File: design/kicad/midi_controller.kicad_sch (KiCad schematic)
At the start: 1 part, among them U1 Teensy4.1

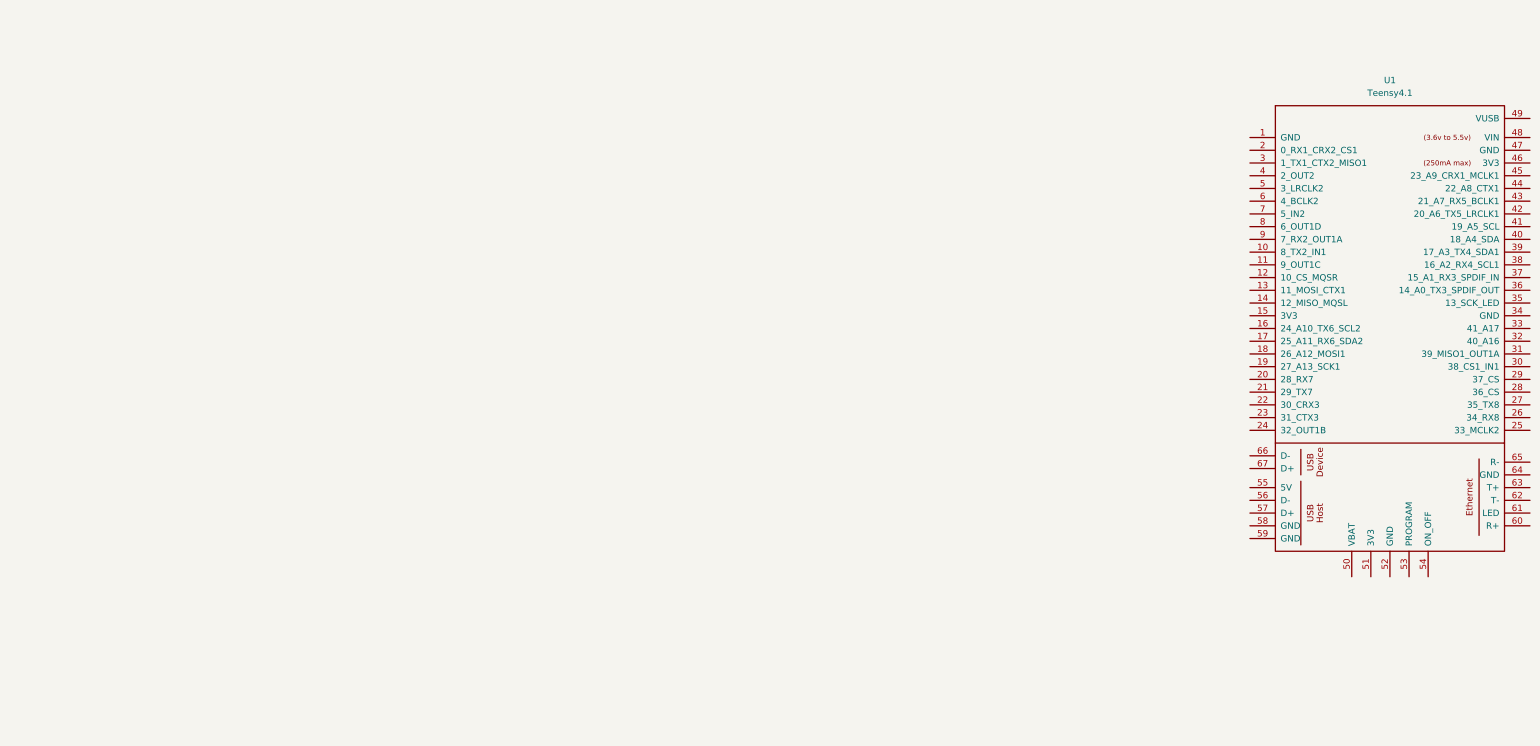
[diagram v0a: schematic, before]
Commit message: Add MIDI Controller component library to KiCad symbol library table
- Introduced a new symbol library for MIDI controllers located at
  "${KIPRJMOD}/component_library/midi_controller/midi_controller.kicad_sym".
- Updated the sym-lib-table to include the new library with a description
  for better organization and accessibility.
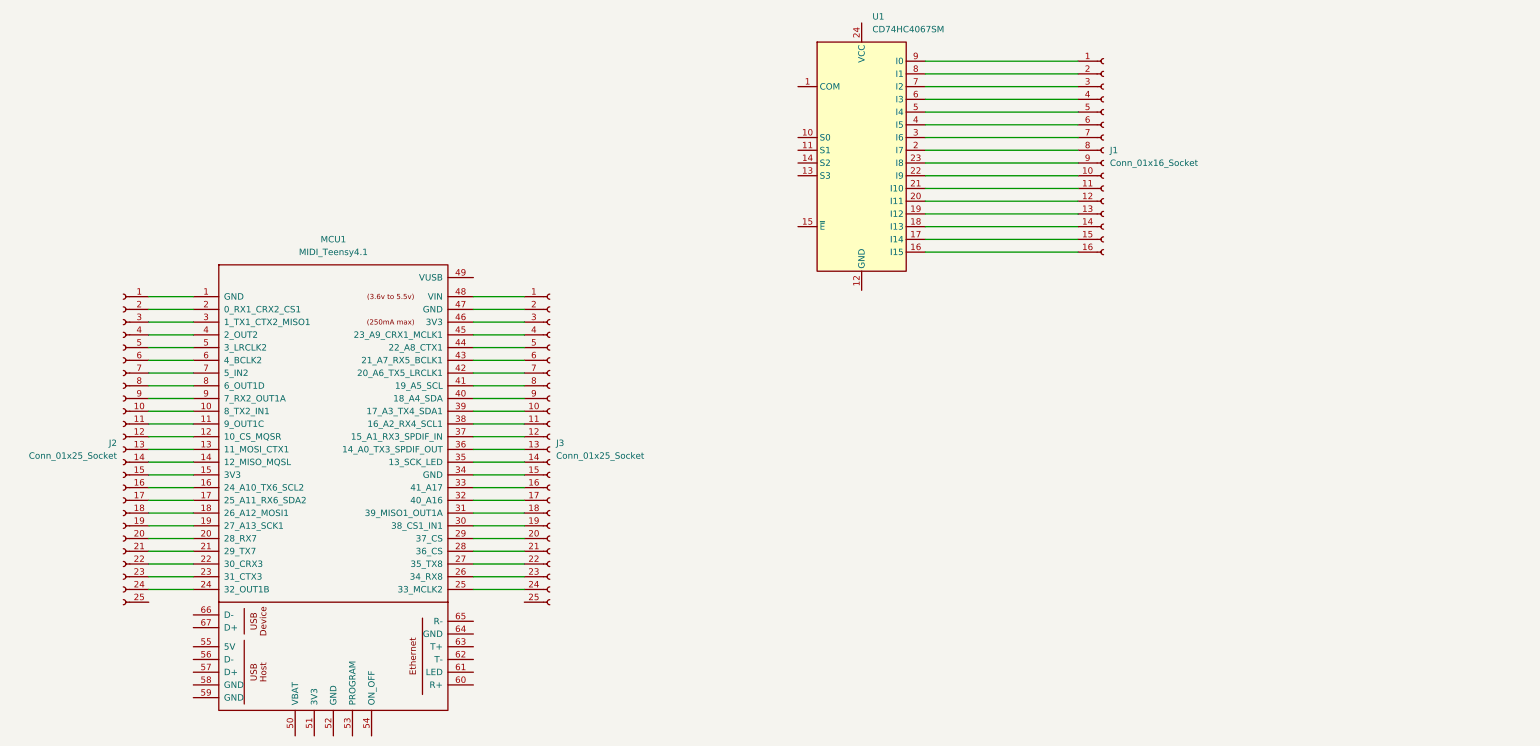
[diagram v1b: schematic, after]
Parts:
- removed U1: Teensy4.1, symbol teensy:Teensy4.1
- added J1: Conn_01x16_Socket, Connector_PinSocket_2.54mm:PinSocket_1x16_P2.54mm_Vertical, symbol Connector:Conn_01x16_Socket
- added J2, J3: Conn_01x25_Socket, Connector_PinSocket_2.54mm:PinSocket_1x25_P2.54mm_Vertical, symbol Connector:Conn_01x25_Socket
- added MCU1: MIDI_Teensy4.1, midi_controller:Teensy41, symbol midi_controller:MIDI_Teensy4.1
- added U1: CD74HC4067SM, Package_SO:SSOP-24_5.3x8.2mm_P0.65mm, symbol 74xx:CD74HC4067SM
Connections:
- new net: J1.1 (Pin_1), U1.9 (I0)
- new net: J1.10 (Pin_10), U1.22 (I9)
- new net: J1.11 (Pin_11), U1.21 (I10)
- new net: J1.12 (Pin_12), U1.20 (I11)
- new net: J1.13 (Pin_13), U1.19 (I12)
- new net: J1.14 (Pin_14), U1.18 (I13)
- new net: J1.15 (Pin_15), U1.17 (I14)
- new net: J1.16 (Pin_16), U1.16 (I15)
- new net: J1.2 (Pin_2), U1.8 (I1)
- new net: J1.3 (Pin_3), U1.7 (I2)
- new net: J1.4 (Pin_4), U1.6 (I3)
- new net: J1.5 (Pin_5), U1.5 (I4)
- new net: J1.6 (Pin_6), U1.4 (I5)
- new net: J1.7 (Pin_7), U1.3 (I6)
- new net: J1.8 (Pin_8), U1.2 (I7)
- new net: J1.9 (Pin_9), U1.23 (I8)
- new net: J2.1 (Pin_1), MCU1.1 (GND)
- new net: J2.10 (Pin_10), MCU1.10 (8_TX2_IN1)
- new net: J2.11 (Pin_11), MCU1.11 (9_OUT1C)
- new net: J2.12 (Pin_12), MCU1.12 (10_CS_MQSR)
- new net: J2.13 (Pin_13), MCU1.13 (11_MOSI_CTX1)
- new net: J2.14 (Pin_14), MCU1.14 (12_MISO_MQSL)
- new net: J2.15 (Pin_15), MCU1.15 (3V3)
- new net: J2.16 (Pin_16), MCU1.16 (24_A10_TX6_SCL2)
- new net: J2.17 (Pin_17), MCU1.17 (25_A11_RX6_SDA2)
- new net: J2.18 (Pin_18), MCU1.18 (26_A12_MOSI1)
- new net: J2.19 (Pin_19), MCU1.19 (27_A13_SCK1)
- new net: J2.2 (Pin_2), MCU1.2 (0_RX1_CRX2_CS1)
- new net: J2.20 (Pin_20), MCU1.20 (28_RX7)
- new net: J2.21 (Pin_21), MCU1.21 (29_TX7)
- new net: J2.22 (Pin_22), MCU1.22 (30_CRX3)
- new net: J2.23 (Pin_23), MCU1.23 (31_CTX3)
- new net: J2.24 (Pin_24), MCU1.24 (32_OUT1B)
- new net: J3.24 (Pin_24), MCU1.25 (33_MCLK2)
- new net: J3.23 (Pin_23), MCU1.26 (34_RX8)
- new net: J3.22 (Pin_22), MCU1.27 (35_TX8)
- new net: J3.21 (Pin_21), MCU1.28 (36_CS)
- new net: J3.20 (Pin_20), MCU1.29 (37_CS)
- new net: J2.3 (Pin_3), MCU1.3 (1_TX1_CTX2_MISO1)
- new net: J3.19 (Pin_19), MCU1.30 (38_CS1_IN1)
- new net: J3.18 (Pin_18), MCU1.31 (39_MISO1_OUT1A)
- new net: J3.17 (Pin_17), MCU1.32 (40_A16)
- new net: J3.16 (Pin_16), MCU1.33 (41_A17)
- new net: J3.15 (Pin_15), MCU1.34 (GND)
- new net: J3.14 (Pin_14), MCU1.35 (13_SCK_LED)
- new net: J3.13 (Pin_13), MCU1.36 (14_A0_TX3_SPDIF_OUT)
- new net: J3.12 (Pin_12), MCU1.37 (15_A1_RX3_SPDIF_IN)
- new net: J3.11 (Pin_11), MCU1.38 (16_A2_RX4_SCL1)
- new net: J3.10 (Pin_10), MCU1.39 (17_A3_TX4_SDA1)
- new net: J2.4 (Pin_4), MCU1.4 (2_OUT2)
- new net: J3.9 (Pin_9), MCU1.40 (18_A4_SDA)
- new net: J3.8 (Pin_8), MCU1.41 (19_A5_SCL)
- new net: J3.7 (Pin_7), MCU1.42 (20_A6_TX5_LRCLK1)
- new net: J3.6 (Pin_6), MCU1.43 (21_A7_RX5_BCLK1)
- new net: J3.5 (Pin_5), MCU1.44 (22_A8_CTX1)
- new net: J3.4 (Pin_4), MCU1.45 (23_A9_CRX1_MCLK1)
- new net: J3.3 (Pin_3), MCU1.46 (3V3)
- new net: J3.2 (Pin_2), MCU1.47 (GND)
- new net: J3.1 (Pin_1), MCU1.48 (VIN)
- new net: J2.5 (Pin_5), MCU1.5 (3_LRCLK2)
- new net: J2.6 (Pin_6), MCU1.6 (4_BCLK2)
- new net: J2.7 (Pin_7), MCU1.7 (5_IN2)
- new net: J2.8 (Pin_8), MCU1.8 (6_OUT1D)
- new net: J2.9 (Pin_9), MCU1.9 (7_RX2_OUT1A)

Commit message: Refactor code structure for improved readability and maintainability
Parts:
- removed J1: Conn_01x16_Socket, Connector_PinSocket_2.54mm:PinSocket_1x16_P2.54mm_Vertical, symbol Connector:Conn_01x16_Socket
- removed J2, J3: Conn_01x25_Socket, Connector_PinSocket_2.54mm:PinSocket_1x25_P2.54mm_Vertical, symbol Connector:Conn_01x25_Socket
- removed U1: CD74HC4067SM, Package_SO:SSOP-24_5.3x8.2mm_P0.65mm, symbol 74xx:CD74HC4067SM
- added D1: MIDI_Display_MSP2807, midi_controller:MSP2807_ILI9341_Display, symbol midi_controller:MIDI_Display_MSP2807
- added ENC_MECH1, ENC_MECH2, ENC_MECH3, ENC_MECH4, ENC_MECH5, ENC_MECH6, ENC_MECH7, ENC_MECH8, ENC_MECH9: MIDI_Encoder_PEC11R, midi_controller:PEC11R4220FS0024, symbol midi_controller:MIDI_Encoder_PEC11R
- added ENC_OPT1: MIDI_Encoder_E38S6G5_Optical, midi_controller:E38S6G5_Optical_Encoder, symbol midi_controller:MIDI_Encoder_E38S6G5_Optical
- added J1, J2: Conn_01x24_Socket, symbol Connector:Conn_01x24_Socket
- added R1: R, Resistor_THT:R_Axial_DIN0204_L3.6mm_D1.6mm_P7.62mm_Horizontal, symbol Device:R
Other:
- moved on the sheet: MCU1

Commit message: Refactor code structure for improved readability and maintainability
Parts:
- removed D1: MIDI_Display_MSP2807, midi_controller:MSP2807_ILI9341_Display, symbol midi_controller:MIDI_Display_MSP2807
- removed ENC_MECH1, ENC_MECH2, ENC_MECH3, ENC_MECH4, ENC_MECH5, ENC_MECH6, ENC_MECH7, ENC_MECH8, ENC_MECH9: MIDI_Encoder_PEC11R, midi_controller:PEC11R4220FS0024, symbol midi_controller:MIDI_Encoder_PEC11R
- removed R1: R, Resistor_THT:R_Axial_DIN0204_L3.6mm_D1.6mm_P7.62mm_Horizontal, symbol Device:R
- added D2: MIDI_Display_MSP2807, midi_controller:MSP2807_ILI9341_Display, symbol midi_controller:MIDI_Display_MSP2807
- added U1: CD74HC4067M, Package_SO:SSOP-24_5.3x8.2mm_P0.65mm, symbol 74xx:CD74HC4067M
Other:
- added sheet Encoder with Push Button_Navigation (encoder_with_push_button.kicad_sch)
- added sheet MIDI_Encoder_Matrix_2x4_with_push_buttons (encoders_2x4_with_push_buttons.kicad_sch)
- moved on the sheet: ENC_OPT1, J1, J2, MCU1

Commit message: Refactor code structure for improved readability and maintainability
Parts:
- added J3: Conn_01x14_Socket, Connector_PinSocket_2.54mm:PinSocket_1x14_P2.54mm_Vertical, symbol Connector:Conn_01x14_Socket
- J1, J2: footprint (none) -> Connector_PinSocket_2.54mm:PinSocket_1x24_P2.54mm_Vertical
- U1: footprint Package_SO:SSOP-24_5.3x8.2mm_P0.65mm -> Package_SO:SOIC-24W_7.5x15.4mm_P1.27mm
- renumbered D2 to D1
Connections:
- net Encoder with Push Button_Navigation/QUAD_A: now also J2.21 (Pin_21)
- net Encoder with Push Button_Navigation/QUAD_B: now also J2.22 (Pin_22)
- net Encoder with Push Button_Navigation/SW_A: now also U1.23 (I8)
- net at J1.1 (Pin_1): now also ENC_OPT1.VCC (+VCC)
- net 2x1.QUAD_A: now reaches J1.10 (Pin_10)
- net 2x1.QUAD_B: now reaches J1.11 (Pin_11)
- net 1x4.QUAD_A: now reaches J1.12 (Pin_12)
- net 1x4.QUAD_B: now reaches J1.13 (Pin_13)
- net at J1.14 (Pin_14): now also J3.7 (Pin_7)
- net at J1.15 (Pin_15): now also ENC_OPT1.0V, ENC_OPT1.GND
- net 1x3.QUAD_A: now reaches J1.16 (Pin_16)
- net 1x3.QUAD_B: now reaches J1.17 (Pin_17)
- net 1x2.QUAD_A: now reaches J1.18 (Pin_18)
- net 1x2.QUAD_B: now reaches J1.19 (Pin_19)
- net Buttons_Momentary/GND: now reaches J1.2 (Pin_2)
- net Buttons_Momentary/GND: now also U1.12 (GND), U1.15 (~{E})
- net at J1.20 (Pin_20): now also J3.5 (Pin_5)
- net 1x1.QUAD_A: now reaches J1.21 (Pin_21)
- net 1x1.QUAD_B: now reaches J1.22 (Pin_22)
- net at J1.23 (Pin_23): now also ENC_OPT1.A
- net at J1.24 (Pin_24): now also ENC_OPT1.B
- net 2x4.QUAD_A: now reaches J1.4 (Pin_4)
- net 2x4.QUAD_B: now reaches J1.5 (Pin_5)
- net 2x3.QUAD_A: now reaches J1.6 (Pin_6)
- net 2x3.QUAD_B: now reaches J1.7 (Pin_7)
- net 2x2.QUAD_A: now reaches J1.8 (Pin_8)
- net 2x2.QUAD_B: now reaches J1.9 (Pin_9)
- net at U1.1 (COM): now also J2.9 (Pin_9)
- net at U1.10 (S0): now also J2.8 (Pin_8)
- net at U1.11 (S1): now also J2.7 (Pin_7)
- net at U1.13 (S3): now also J2.5 (Pin_5)
- net at U1.14 (S2): now also J2.6 (Pin_6)
- net Buttons_Momentary/BUTTON_PUSH_MOM_06: now reaches U1.17 (I14)
- net Buttons_Momentary/BUTTON_PUSH_MOM_05: now reaches U1.18 (I13)
- net Buttons_Momentary/BUTTON_PUSH_MOM_04: now reaches U1.19 (I12)
- net MIDI_Encoder_Matrix_2x4_with_push_buttons/2x4_SW_A: now reaches U1.2 (I7)
- net Buttons_Momentary/BUTTON_PUSH_MOM_03: now reaches U1.20 (I11)
- net Buttons_Momentary/BUTTON_PUSH_MOM_02: now reaches U1.21 (I10)
- net Buttons_Momentary/BUTTON_PUSH_MOM_01: now reaches U1.22 (I9)
- net MIDI_Encoder_Matrix_2x4_with_push_buttons/2x3_SW_A: now reaches U1.3 (I6)
- net MIDI_Encoder_Matrix_2x4_with_push_buttons/2x2_SW_A: now reaches U1.4 (I5)
- net MIDI_Encoder_Matrix_2x4_with_push_buttons/2x1_SW_A: now reaches U1.5 (I4)
- net MIDI_Encoder_Matrix_2x4_with_push_buttons/1x4_SW_A: now reaches U1.6 (I3)
- net MIDI_Encoder_Matrix_2x4_with_push_buttons/1x3_SW_A: now reaches U1.7 (I2)
- net MIDI_Encoder_Matrix_2x4_with_push_buttons/1x2_SW_A: now reaches U1.8 (I1)
- net MIDI_Encoder_Matrix_2x4_with_push_buttons/1x1_SW_A: now reaches U1.9 (I0)
- net at J2.1 (Pin_1): now also J3.2 (Pin_2)
- net at J2.10 (Pin_10): now also J3.8 (Pin_8)
- net at J2.11 (Pin_11): now also J3.4 (Pin_4)
- net at J2.12 (Pin_12): now also J3.3 (Pin_3)
- net at J2.13 (Pin_13): now also J3.6 (Pin_6)
- net at J2.14 (Pin_14): now also J3.9 (Pin_9)
- net at J2.15 (Pin_15): now also J3.1 (Pin_1)
- net at J2.16 (Pin_16): now also J3.14 (Pin_14)
- net at J2.18 (Pin_18): now also J3.12 (Pin_12)
- net at J2.19 (Pin_19): now also J3.10 (Pin_10)
- net at J2.20 (Pin_20): now also J3.11 (Pin_11)
- net at J2.3 (Pin_3): now also J3.13 (Pin_13)
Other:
- added sheet Buttons_Momentary (buttons_momentary.kicad_sch)
- sheet MIDI_Encoder_Matrix_2x4_with_push_buttons ports: added 1x1_SW_A, 1x1{QUAD_A QUAD_B}, 1x2_SW_A, 1x2{QUAD_A QUAD_B}, 1x3_SW_A, 1x3{QUAD_A QUAD_B}, 1x4_SW_A, 1x4{QUAD_A QUAD_B}, 2x1_SW_A, 2x1{QUAD_A QUAD_B}, 2x2_SW_A, 2x2{QUAD_A QUAD_B}, 2x3_SW_A, 2x3{QUAD_A QUAD_B}, 2x4_SW_A, 2x4{QUAD_A QUAD_B}; removed 1x1{QUAD_A QUAD_B SW}, 1x2{QUAD_A QUAD_B SW}, 1x3{QUAD_A QUAD_B SW}, 1x4{QUAD_A QUAD_B SW}, 2x1{QUAD_A QUAD_B SW}, 2x2{QUAD_A QUAD_B SW}, 2x3{QUAD_A QUAD_B SW}, 2x4{QUAD_A QUAD_B SW}
- moved on the sheet: D1, ENC_OPT1, J1, J2, MCU1, U1

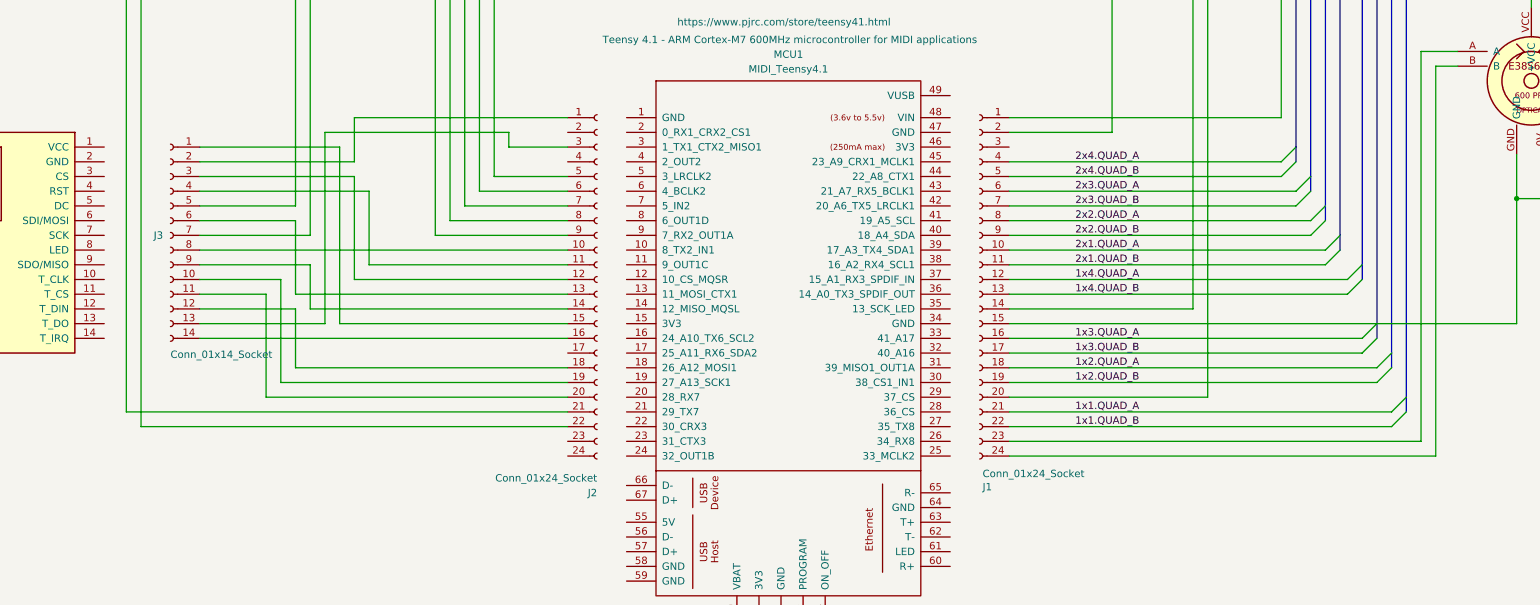
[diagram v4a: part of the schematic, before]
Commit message: Update kicad binary files - Update Teensy 3d models - set default env to prod
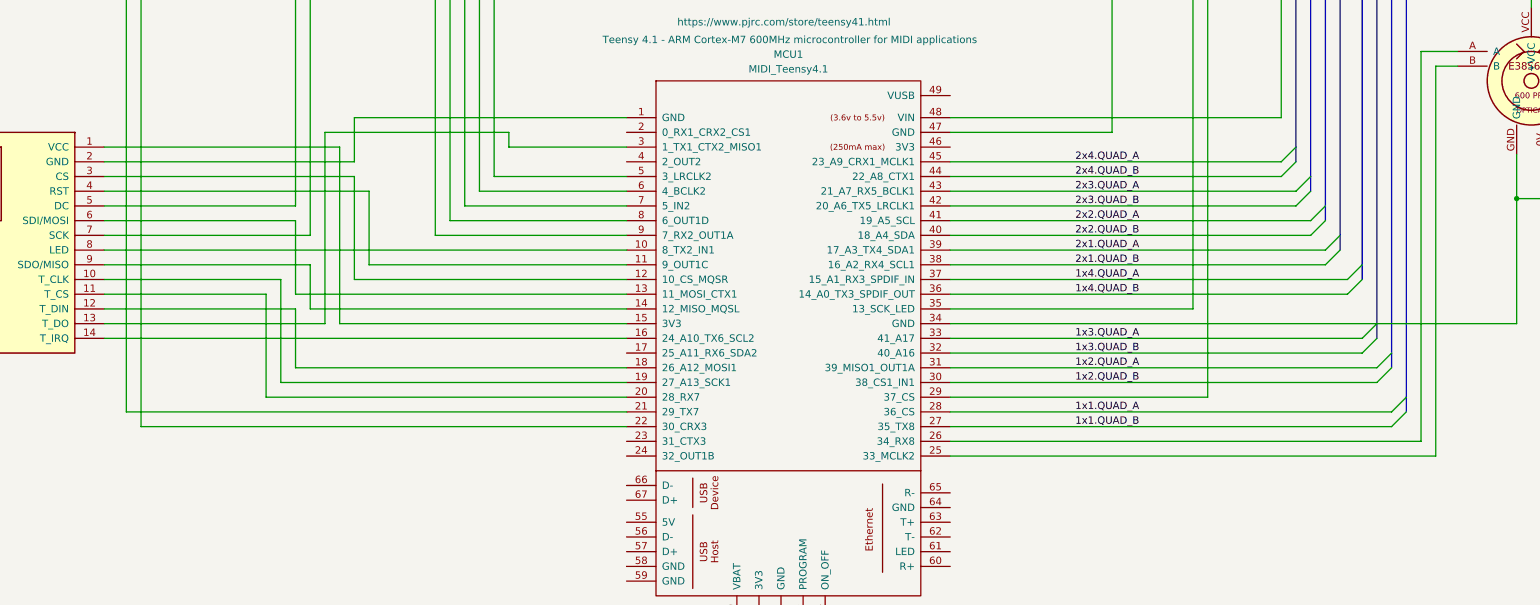
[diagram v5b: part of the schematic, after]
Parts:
- removed J1, J2: Conn_01x24_Socket, Connector_PinSocket_2.54mm:PinSocket_1x24_P2.54mm_Vertical, symbol Connector:Conn_01x24_Socket
- removed J3: Conn_01x14_Socket, Connector_PinSocket_2.54mm:PinSocket_1x14_P2.54mm_Vertical, symbol Connector:Conn_01x14_Socket
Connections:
- net 1x1.QUAD_A: now also MCU1.28 (36_CS)
- net 1x1.QUAD_B: now also MCU1.27 (35_TX8)
- net 1x2.QUAD_A: now also MCU1.31 (39_MISO1_OUT1A)
- net 1x2.QUAD_B: now also MCU1.30 (38_CS1_IN1)
- net 1x3.QUAD_A: now also MCU1.33 (41_A17)
- net 1x3.QUAD_B: now also MCU1.32 (40_A16)
- net 1x4.QUAD_A: now also MCU1.37 (15_A1_RX3_SPDIF_IN)
- net 1x4.QUAD_B: now also MCU1.36 (14_A0_TX3_SPDIF_OUT)
- net 2x1.QUAD_A: now also MCU1.39 (17_A3_TX4_SDA1)
- net 2x1.QUAD_B: now also MCU1.38 (16_A2_RX4_SCL1)
- net 2x2.QUAD_A: now also MCU1.41 (19_A5_SCL)
- net 2x2.QUAD_B: now also MCU1.40 (18_A4_SDA)
- net 2x3.QUAD_A: now also MCU1.43 (21_A7_RX5_BCLK1)
- net 2x3.QUAD_B: now also MCU1.42 (20_A6_TX5_LRCLK1)
- net 2x4.QUAD_A: now also MCU1.45 (23_A9_CRX1_MCLK1)
- net 2x4.QUAD_B: now also MCU1.44 (22_A8_CTX1)
- net Buttons_Momentary/GND: now also MCU1.47 (GND)
- net Encoder with Push Button_Navigation/QUAD_A: now also MCU1.21 (29_TX7)
- net Encoder with Push Button_Navigation/QUAD_B: now also MCU1.22 (30_CRX3)
- net at ENC_OPT1.VCC (+VCC): now also MCU1.48 (VIN)
- net at ENC_OPT1.0V, ENC_OPT1.GND: now also MCU1.34 (GND)
- net at ENC_OPT1.A: now also MCU1.26 (34_RX8)
- net at ENC_OPT1.B: now also MCU1.25 (33_MCLK2)
- net at D1.1 (VCC): now also MCU1.15 (3V3)
- net at D1.10 (T_CLK): now also MCU1.19 (27_A13_SCK1)
- net at D1.11 (T_CS): now also MCU1.20 (28_RX7)
- net at D1.12 (T_DIN): now also MCU1.18 (26_A12_MOSI1)
- net at D1.13 (T_DO): now also MCU1.3 (1_TX1_CTX2_MISO1)
- net at D1.14 (T_IRQ): now also MCU1.16 (24_A10_TX6_SCL2)
- net at D1.2 (GND): now also MCU1.1 (GND)
- net at D1.3 (CS): now also MCU1.12 (10_CS_MQSR)
- net at D1.4 (RST): now also MCU1.11 (9_OUT1C)
- net at D1.5 (DC): now also MCU1.29 (37_CS)
- net at D1.6 (SDI/MOSI): now also MCU1.13 (11_MOSI_CTX1)
- net at D1.7 (SCK): now also MCU1.35 (13_SCK_LED)
- net at D1.8 (LED): now also MCU1.10 (8_TX2_IN1)
- net at D1.9 (SDO/MISO): now also MCU1.14 (12_MISO_MQSL)
- net at U1.1 (COM): now also MCU1.9 (7_RX2_OUT1A)
- net at U1.10 (S0): now also MCU1.8 (6_OUT1D)
- net at U1.11 (S1): now also MCU1.7 (5_IN2)
- net at U1.13 (S3): now also MCU1.5 (3_LRCLK2)
- net at U1.14 (S2): now also MCU1.6 (4_BCLK2)
